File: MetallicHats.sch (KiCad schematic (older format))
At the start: 36 parts, among them Q1 J113, U1 40106, U2 TL072

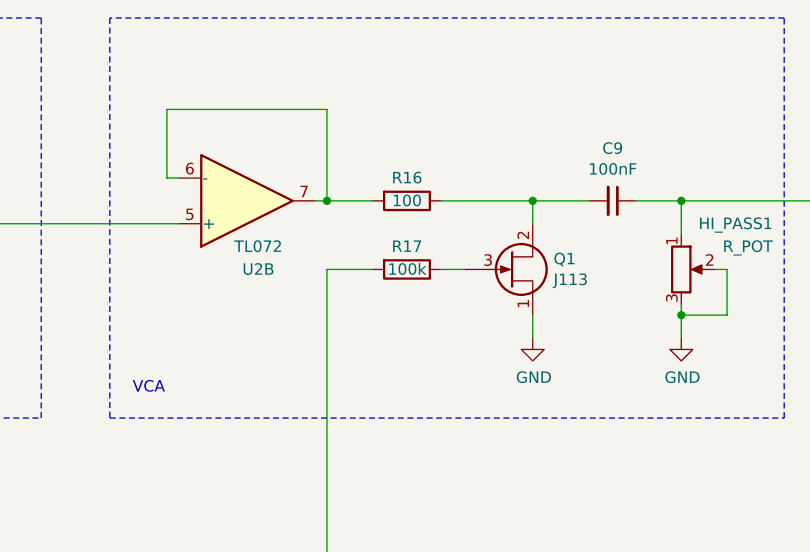
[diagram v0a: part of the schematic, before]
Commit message: Added LED on VCA
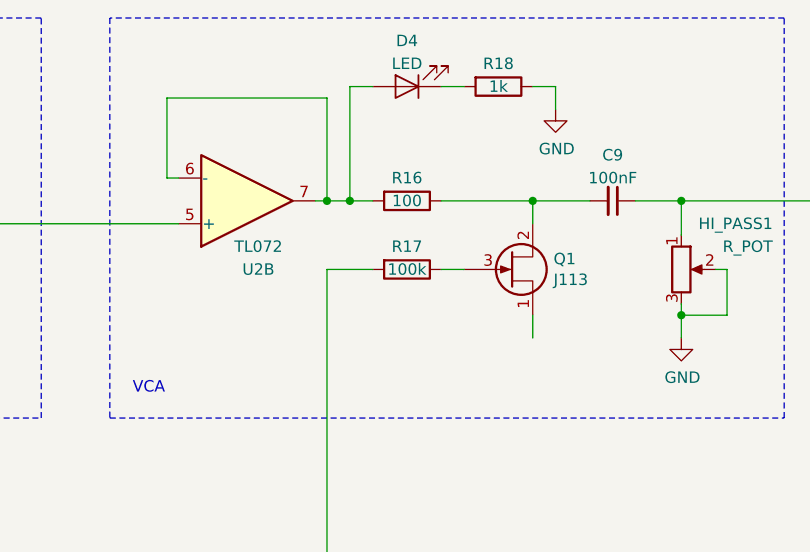
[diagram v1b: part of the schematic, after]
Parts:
- added D4: LED, symbol Device:LED
- added R18: 1k, symbol Device:R
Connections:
- net GND: now also R18.1; no longer Q1.1 (S)
- net at R16.2, U2.6 (-), U2.7: now also D4.2 (A)
- new net: D4.1 (K), R18.2
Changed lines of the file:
@@
 EESchema Schematic File Version 4
+LIBS:MetallicHats-cache
 EELAYER 26 0
 EELAYER END
@@
 	5900 1550 5850 1550
 Wire Wire Line
-	5850 1550 5850 1250
-Wire Wire Line
-	5850 1250 6550 1250
-Wire Wire Line
-	6550 1250 6550 1650
+	5850 1550 5850 1200
 Wire Wire Line
 	6550 1650 6500 1650
@@
 	1    0    0    -1
 $EndComp
-$Comp
-L power:GND #PWR06
-U 1 1 60B2F183
-P 7450 2250
-F 0 "#PWR06" H 7450 2000 50  0001 C CNN
-F 1 "GND" H 7455 2077 50  0000 C CNN
-F 2 "" H 7450 2250 50  0001 C CNN
-F 3 "" H 7450 2250 50  0001 C CNN
-	1    7450 2250
-	1    0    0    -1
-$EndComp
 Wire Wire Line
 	7450 2150 7450 2250
@@
 U 1 1 60C1D554
 P 7800 1650
-F 0 "C9" V 7571 1650 50  0000 C CNN
-F 1 "100nF" V 7662 1650 50  0000 C CNN
+F 0 "C9" V 7600 1650 50  0000 C CNN
+F 1 "100nF" V 7700 1650 50  0000 C CNN
 F 2 "" H 7800 1650 50  0001 C CNN
 F 3 "~" H 7800 1650 50  0001 C CNN
@@
 Connection ~ 7450 1650
 Wire Wire Line
-	6550 1650 6750 1650
+	6550 1650 6650 1650
 Connection ~ 6550 1650
 Wire Wire Line
@@
 	6050 6850 6050 6950
 $Comp
-L power:+9V #PWR?
+L power:+9V #PWR06
 U 1 1 60D3880D
 P 5450 5900
-F 0 "#PWR?" H 5450 5750 50  0001 C CNN
+F 0 "#PWR06" H 5450 5750 50  0001 C CNN
 F 1 "+9V" H 5465 6073 50  0000 C CNN
 F 2 "" H 5450 5900 50  0001 C CNN
@@
 $EndComp
 $Comp
-L power:GND #PWR?
+L power:GND #PWR08
 U 1 1 60D3889D
 P 5450 6800
-F 0 "#PWR?" H 5450 6550 50  0001 C CNN
+F 0 "#PWR08" H 5450 6550 50  0001 C CNN
 F 1 "GND" H 5455 6627 50  0000 C CNN
 F 2 "" H 5450 6800 50  0001 C CNN
@@
 Wire Wire Line
 	4150 4900 4050 4900
+$Comp
+L Device:LED D4
+U 1 1 60948A7A
+P 6900 1150
+F 0 "D4" H 6900 950 50  0000 C CNN
+F 1 "LED" H 6900 1050 50  0000 C CNN
+F 2 "" H 6900 1150 50  0001 C CNN
+F 3 "~" H 6900 1150 50  0001 C CNN
+	1    6900 1150
+	-1   0    0    1
+$EndComp
+Wire Wire Line
+	5850 1200 6550 1200
+Wire Wire Line
+	6550 1200 6550 1650
+Wire Wire Line
+	6750 1150 6650 1150
+Wire Wire Line
+	6650 1150 6650 1650
+Connection ~ 6650 1650
+Wire Wire Line
+	6650 1650 6750 1650
+$Comp
+L Device:R R18
+U 1 1 6099A208
+P 7300 1150
+F 0 "R18" V 7200 1150 50  0000 C CNN
+F 1 "1k" V 7300 1150 50  0000 C CNN
+F 2 "" V 7230 1150 50  0001 C CNN
+F 3 "~" H 7300 1150 50  0001 C CNN
+	1    7300 1150
+	0    1    1    0
+$EndComp
+Wire Wire Line
+	7050 1150 7150 1150
+$Comp
+L power:GND #PWR09
+U 1 1 609A5FF6
+P 7550 1250
+F 0 "#PWR09" H 7550 1000 50  0001 C CNN
+F 1 "GND" H 7555 1077 50  0000 C CNN
+F 2 "" H 7550 1250 50  0001 C CNN
+F 3 "" H 7550 1250 50  0001 C CNN
+	1    7550 1250
+	1    0    0    -1
+$EndComp
+Wire Wire Line
+	7450 1150 7550 1150
+Wire Wire Line
+	7550 1150 7550 1250
 $EndSCHEMATC

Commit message: Fixedp pot values
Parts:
- DECAY1: value R_POT -> B1M
- HI_PASS1: value R_POT -> B10K
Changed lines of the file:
@@
 P 4500 1200
 F 0 "DECAY1" V 4386 1200 50  0000 C CNN
-F 1 "R_POT" V 4295 1200 50  0000 C CNN
+F 1 "B1M" V 4295 1200 50  0000 C CNN
 F 2 "" H 4500 1200 50  0001 C CNN
 F 3 "~" H 4500 1200 50  0001 C CNN
@@
 P 8100 1950
 F 0 "HI_PASS1" H 8500 2150 50  0000 R CNN
-F 1 "R_POT" H 8500 2050 50  0000 R CNN
+F 1 "B10K" H 8500 2050 50  0000 R CNN
 F 2 "" H 8100 1950 50  0001 C CNN
 F 3 "~" H 8100 1950 50  0001 C CNN

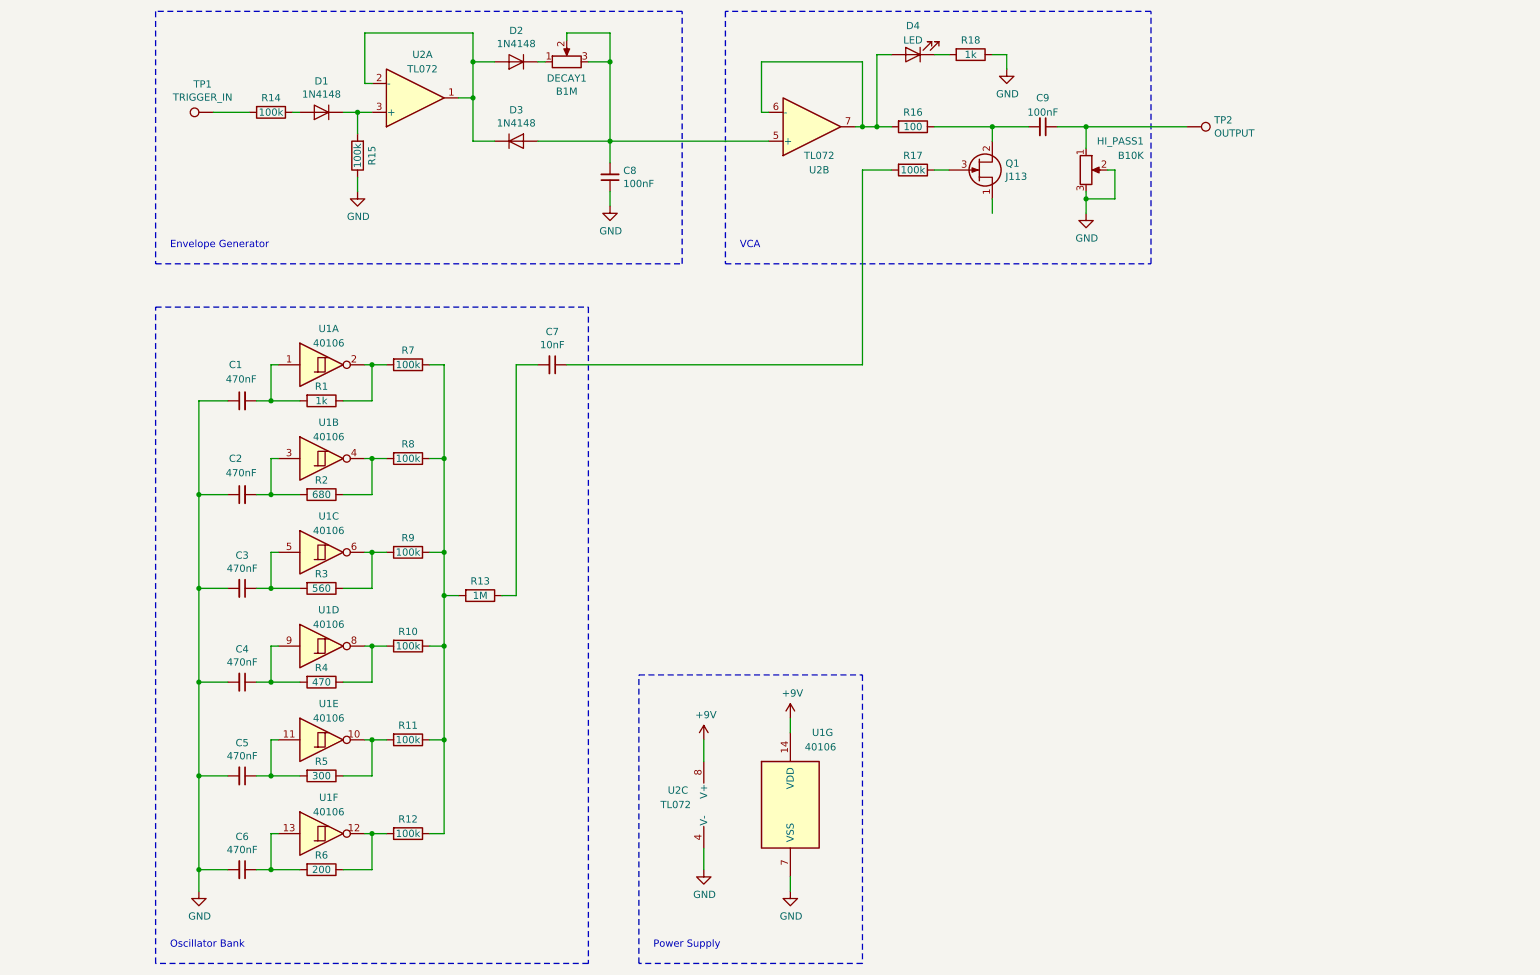
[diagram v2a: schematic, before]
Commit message: Added version vactrol circuit
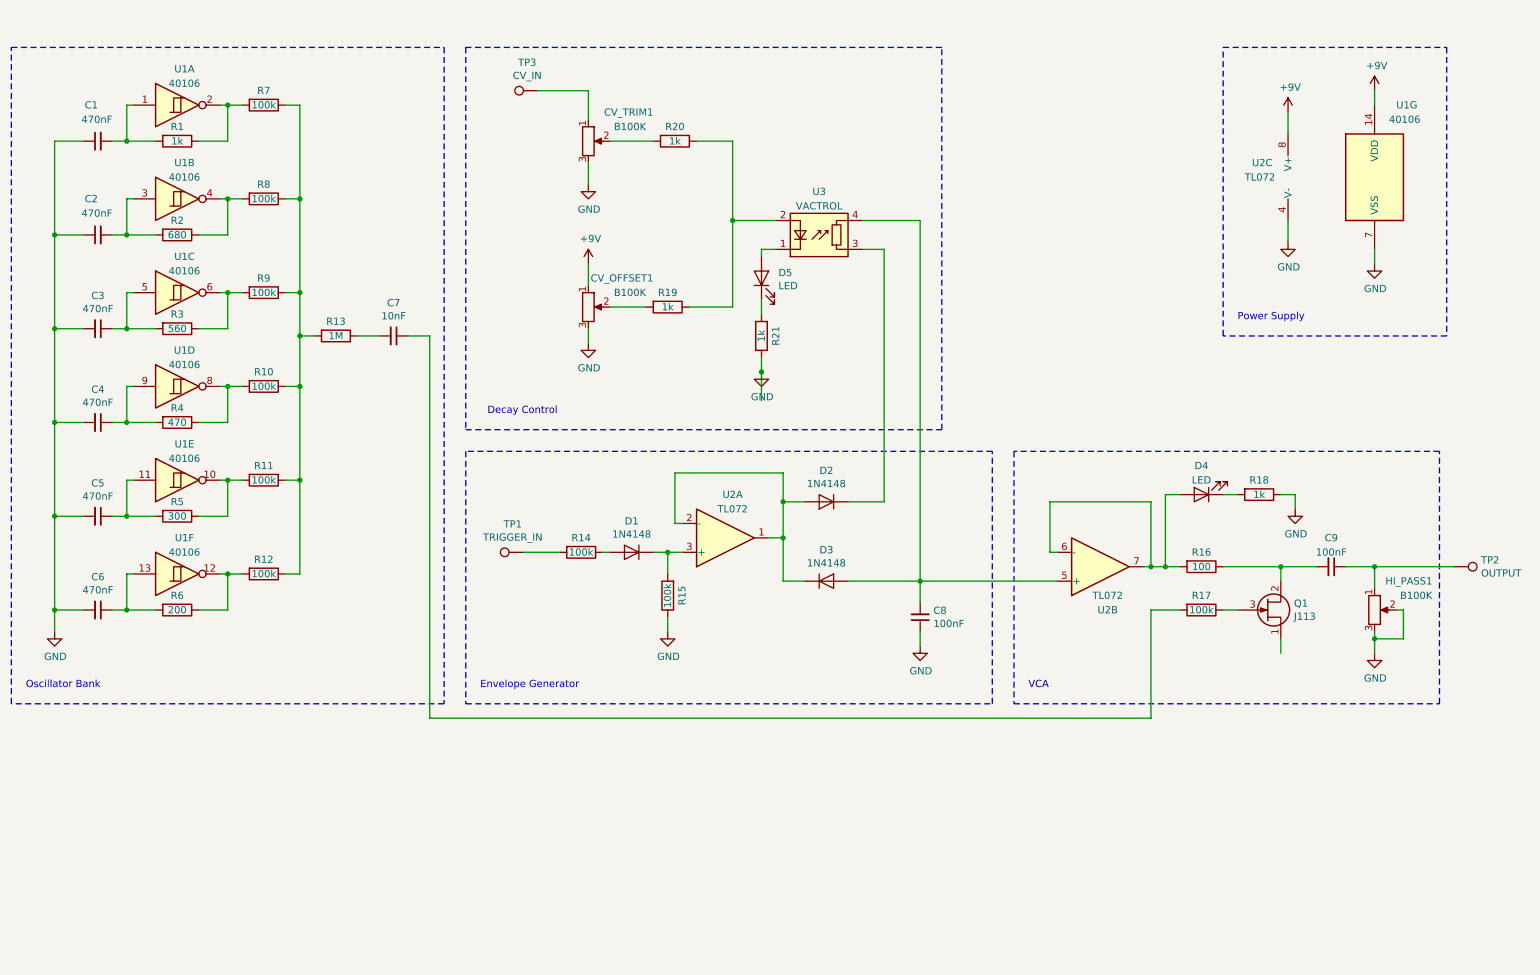
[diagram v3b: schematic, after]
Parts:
- removed DECAY1: B1M, symbol Device:R_POT
- added CV_OFFSET1, CV_TRIM1: B100K, symbol Device:R_POT
- added D5: LED, symbol Device:LED
- added R19, R20, R21: 1k, symbol Device:R
- added TP3: CV_IN, symbol Connector:TestPoint
- added U3: VACTROL, OptoDevice:PerkinElmer_VTL5C, symbol Isolator:VTL5C
- HI_PASS1: value B10K -> B100K
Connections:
- net +9V: now also CV_OFFSET1.1
- net GND: now also CV_OFFSET1.3, CV_TRIM1.3, R21.1
- net at C8.2, D3.2 (A), U2.5 (+): now also U3.4
- net at D2.1 (K): now also U3.3
- new net: D5.2 (A), U3.1 (-)
- new net: R19.1, R20.1, U3.2 (+)
- new net: CV_OFFSET1.2, R19.2
- new net: CV_TRIM1.2, R20.2
- new net: CV_TRIM1.1, TP3.1
- new net: D5.1 (K), R21.2
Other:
- note added: "Decay Control"
- moved on the sheet: C1, C2, C3, C4, C5, C6, C7, C8, C9, D1, D2, D3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
